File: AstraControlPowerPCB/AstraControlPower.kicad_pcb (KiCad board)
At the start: 4 copper layers, 32 x 92 mm, 47 parts, among them CN1 WJ124_5P, CN2 WJ124_5P, CN3 WJ124_5P, CN4 WJ124_5P, CN5 WJ124_5P, CN6 WJ124_5P

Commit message: Updated rotation
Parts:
- turned CN1 to 0 degrees
- turned CN3 to 180 degrees
- turned CN4 to 0 degrees
- turned CN6 to 180 degrees

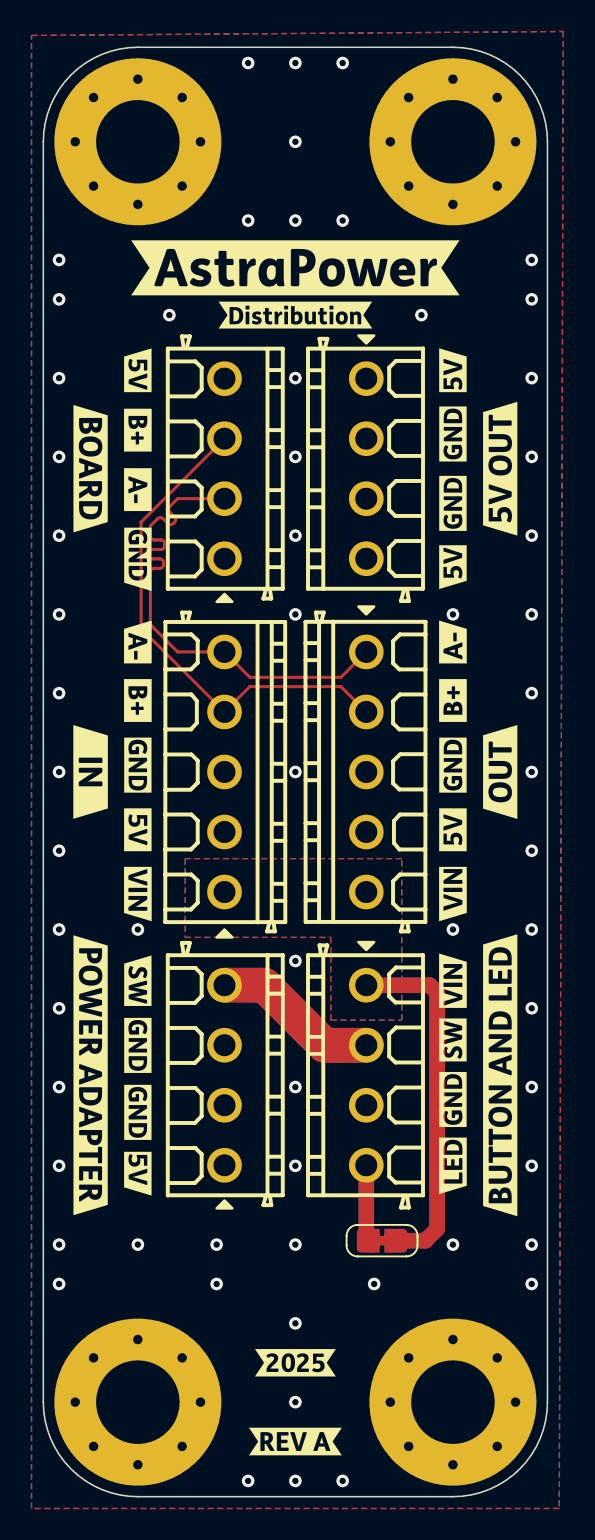
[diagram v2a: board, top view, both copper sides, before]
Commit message: Update to 180 rot 4pin
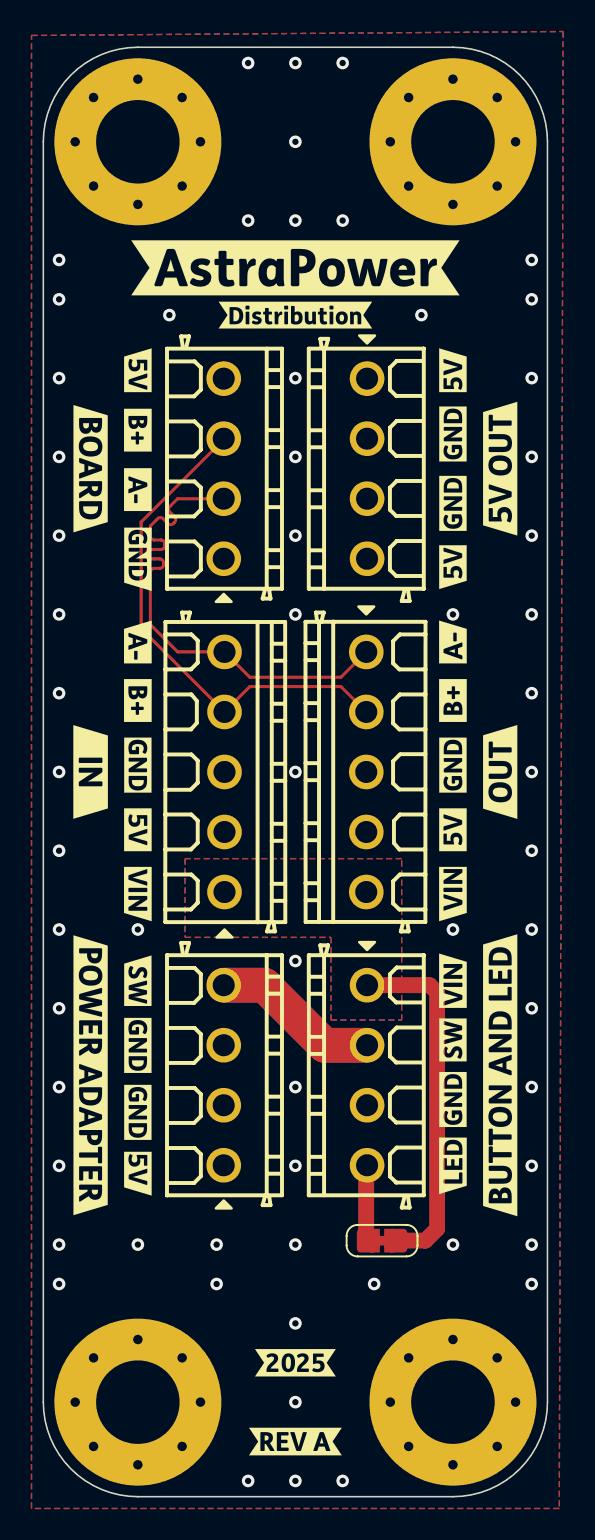
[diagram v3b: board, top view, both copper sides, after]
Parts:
- turned CN1 to 180 degrees
- turned CN3 to 0 degrees
- turned CN4 to 180 degrees
- turned CN6 to 0 degrees
